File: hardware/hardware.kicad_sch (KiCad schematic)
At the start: 14 parts, among them J1 AVR-ISP-6, U1 AMS1117-3.3, U2 ATmega88PA-A, U3 CH340C, U4 MPU-6050, Y1 Crystal

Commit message: up
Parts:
- removed C2: C, Capacitor_SMD:C_0603_1608Metric, symbol Device:C
- removed U1: AMS1117-3.3, Package_TO_SOT_SMD:SOT-223-3_TabPin2, symbol Regulator_Linear:AMS1117-3.3
- added C6: C, Capacitor_SMD:C_0603_1608Metric, symbol Device:C
- added U6: AP2112K-3.3, Package_TO_SOT_SMD:SOT-23-5, symbol Regulator_Linear:AP2112K-3.3
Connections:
- net +BATT is gone; now on net +3V3: C1.1
- net +3V3: now also U6.5 (VOUT)
- net +5V: now also C6.1, U6.1 (VIN), U6.3 (EN)
- net GND: now also C6.2, U6.2 (GND)
- net MPU_IRQ: now also U2.30 (PD0)
- net A0: no longer names the net of U2.23 (PC0)
- net A1: no longer names the net of U2.24 (PC1)
- net A2: no longer names the net of U2.25 (PC2)
- net AL: no longer names the net of U2.13 (PB1)
- net BL: no longer names the net of U2.14 (PB2)
- net PWM: no longer names the net of U2.12 (PB0)

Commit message: up
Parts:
- added C10, C11, C2: C, Capacitor_SMD:C_0603_1608Metric, symbol Device:C
- added J2, J3, J4: Conn_01x08_MountingPin, Connector_PinHeader_2.54mm:PinHeader_1x08_P2.54mm_Vertical, symbol Connector_Generic_MountingPin:Conn_01x08_MountingPin
- Y1: footprint Crystal:Crystal_SMD_HC49-SD -> Crystal:Crystal_SMD_Abracon_ABM7-2Pin_6.0x3.5mm
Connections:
- net +5V: now also U2.20 (AREF), C10.1, C11.1, C2.1, J4.8 (Pin_8)
- net GND: now also C10.2, C11.2, C2.2, J3.8 (Pin_8)
- net MISO: now also J4.5 (Pin_5)
- net MOSI: now also J4.4 (Pin_4)
- net MPU_IRQ: now also U2.32 (PD2), J2.3 (Pin_3); no longer U2.30 (PD0)
- net SCK: now also J4.6 (Pin_6)
- net PD3: now reaches U2.1 (PD3)
- net PD3: now also J2.4 (Pin_4)
- net PD6: now reaches U2.10 (PD6)
- net PD6: now also J2.7 (Pin_7)
- net PD7: now reaches U2.11 (PD7)
- net PD7: now also J2.8 (Pin_8)
- net PB0: now reaches U2.12 (PB0)
- net PB0: now also J4.1 (Pin_1)
- net PB1: now reaches U2.13 (PB1)
- net PB1: now also J4.2 (Pin_2)
- net PB2: now reaches U2.14 (PB2)
- net PB2: now also J4.3 (Pin_3)
- net PD4: now reaches U2.2 (PD4)
- net PD4: now also J2.5 (Pin_5)
- net PC0: now reaches U2.23 (PC0)
- net PC0: now also J3.1 (Pin_1)
- net PC1: now reaches U2.24 (PC1)
- net PC1: now also J3.2 (Pin_2)
- net PC2: now reaches U2.25 (PC2)
- net PC2: now also J3.3 (Pin_3)
- net PC3: now reaches U2.26 (PC3)
- net PC3: now also J3.4 (Pin_4)
- net PC4: now reaches U2.27 (PC4)
- net PC4: now also J3.5 (Pin_5)
- net PC5: now reaches U2.28 (PC5)
- net PC5: now also J3.6 (Pin_6)
- net PD1: now reaches U2.31 (PD1)
- net PD1: now also J2.2 (Pin_2)
- net PD5: now reaches U2.9 (PD5)
- net PD5: now also J2.6 (Pin_6)
- net RST renamed PC6
- net PC6: now also J3.7 (Pin_7)
- new net PD0: J2.1 (Pin_1), U2.30 (PD0)
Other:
- moved on the sheet: J1

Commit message: up
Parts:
- added C12, C13: 1u, Capacitor_SMD:C_0603_1608Metric, symbol Device:C_Small
- added D1, D2: LED, Diode_SMD:D_0603_1608Metric, symbol Device:LED
- added J5: USB_B_Micro, Connector_USB:USB_Micro-B_GCT_USB3076-30-A, symbol Connector:USB_B_Micro
- added R1, R2, R5, R6: 10k, Resistor_SMD:R_0603_1608Metric, symbol Device:R_Small
- added R3, R4: 4.7k, Resistor_SMD:R_0603_1608Metric, symbol Device:R_Small
- added SW1, SW2: SW_Push, Button_Switch_SMD:SW_Push_SPST_NO_Alps_SKRK, symbol Switch:SW_Push
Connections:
- net SCL is gone; now on net PC5: U4.23 (SCL)
- net SDA is gone; now on net PC4: U4.24 (SDA)
- net +5V: now also J5.1 (VBUS), R2.1, R5.1, R6.1
- net D+: now also J5.3 (D+)
- net D-: now also J5.2 (D-)
- net GND: now also C12.2, C13.2, D1.1 (K), D2.1 (K), J5.5 (GND), R3.1, R4.1, SW1.1, SW2.1
- net PB0: now also C13.1, R6.2, SW2.2
- net PC4: now also R3.2
- net PC5: now also R4.2
- net PC6: now also C12.1, R5.2, SW1.2
- net SCK: now also R1.1
- new net: D2.2 (A), R2.2
- new net: D1.2 (A), R1.2

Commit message: finish wiring
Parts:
- Y1: footprint Crystal:Crystal_SMD_Abracon_ABM7-2Pin_6.0x3.5mm -> Crystal:Crystal_SMD_2012-2Pin_2.0x1.2mm
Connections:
- net RX-PROG is gone; now on net PD1: U3.3 (RXD)
- net TX-PROG is gone; now on net PD0: U3.2 (TXD)
- net +3V3: now also J4.7 (Pin_7); no longer C5.1, U3.16 (VCC), U3.4 (V3)
- net +5V: now also C5.1, U3.16 (VCC)

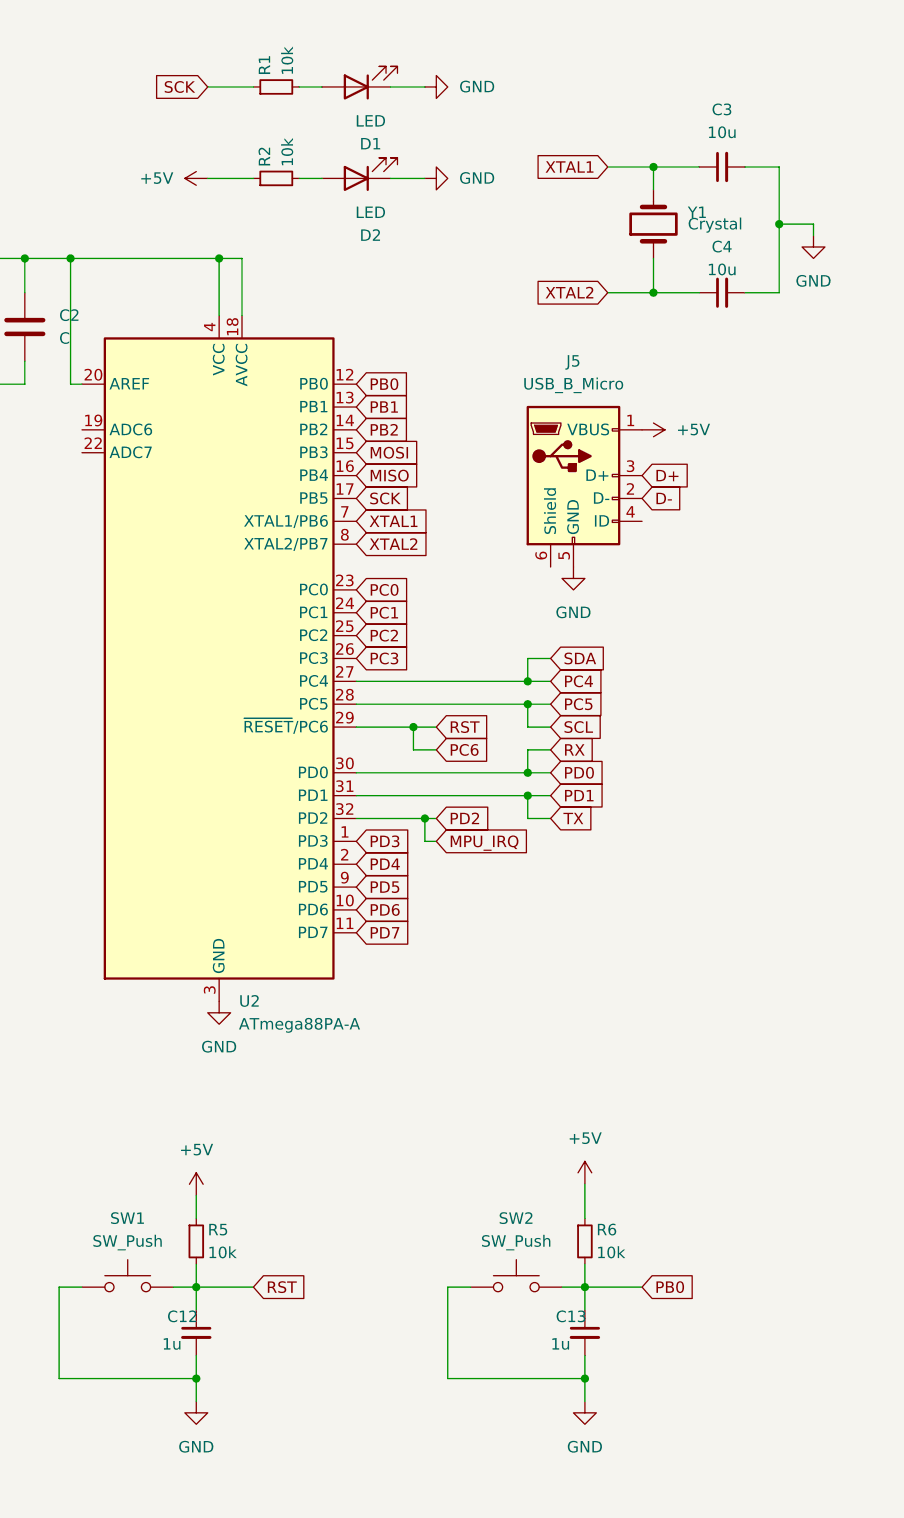
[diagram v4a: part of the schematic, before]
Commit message: update parts lcsc
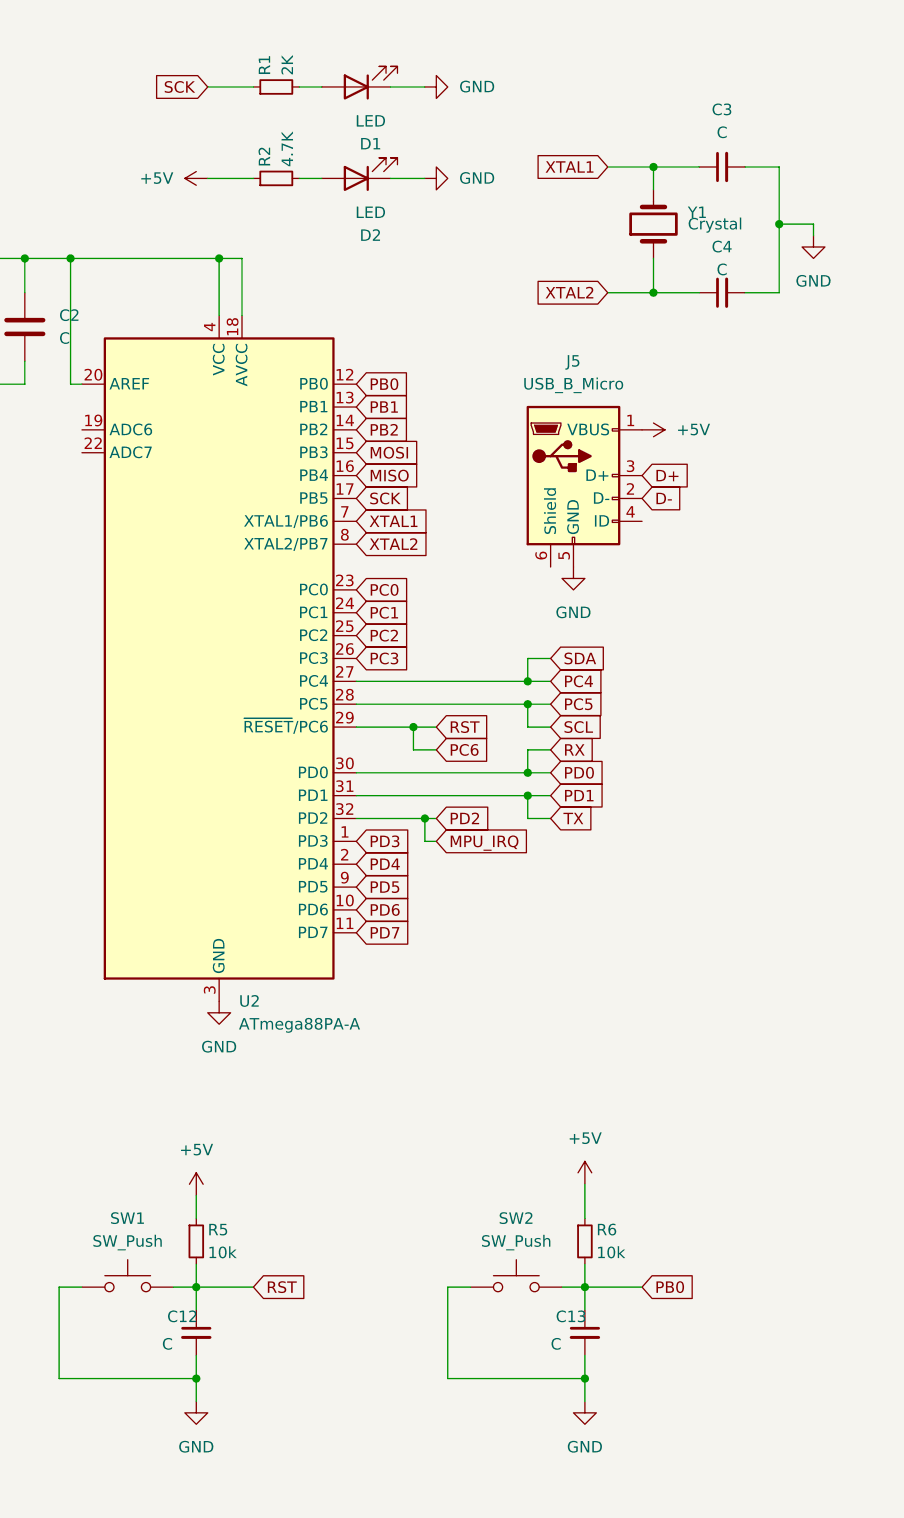
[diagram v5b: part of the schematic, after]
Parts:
- C1, C10, C6: LCSC (none) -> C14858
- C11, C2, C7: LCSC (none) -> C5137611
- C12, C13: value 1u -> C; LCSC (none) -> C5137611
- C3, C4: value 10u -> C; LCSC (none) -> C106245
- C5: LCSC (none) -> C106245
- C8: LCSC (none) -> C1322361
- C9: LCSC (none) -> C1604
- D1: LCSC (none) -> C965799
- D2: LCSC (none) -> C965807
- J5: LCSC (none) -> C6007475
- R1: value 10k -> 2K; LCSC (none) -> C22975
- R2: value 10k -> 4.7K; LCSC (none) -> C99782
- R3, R4: LCSC (none) -> C99782
- R5, R6: LCSC (none) -> C2930027
- SW1, SW2: LCSC (none) -> C115357
- U2: LCSC (none) -> C8727
- U3: LCSC (none) -> C84681
- U4: LCSC (none) -> C24112
- U6: LCSC (none) -> C51118
- Y1: footprint Crystal:Crystal_SMD_2012-2Pin_2.0x1.2mm -> Crystal:Crystal_SMD_3225-4Pin_3.2x2.5mm; LCSC (none) -> C2682775
